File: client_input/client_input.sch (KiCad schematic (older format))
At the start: 21 parts, among them P1 CONN_01X06, P2 CONN_01X08, SW1 DIPS_08, SW2 SW_PUSH, SW3 SW_PUSH, U1 ESP-12_Breakout, U2 MCP23017, U3 MCP3208, U4 WS2812B

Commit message: updated references, added BattSense, fixed errors
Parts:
- removed P?: CONN_01X05, symbol CONN_01X05
- added P7: spare I/O, symbol CONN_01X04
- added R1: 100k, symbol R
- added R2: 22k, symbol R
- added SW4: PAIR_MODE, Buttons_Switches_ThroughHole:SW_TH_Tactile_Omron_B3F-10xx, symbol SW_PUSH
- P1: renamed from P2; value CONN_01X08 -> Analog In
- P2: renamed from P1; value CONN_01X06 -> FTDI
- P3, P4: renamed from P?; value CONN_01X09 -> Ribbon
- P5, P6: renamed from P?; value CONN_01X03 -> Ribbon
- SW2: value SW_PUSH -> RESET
- SW3: value SW_PUSH -> Bootload
- gave numbers to parts that had none: 6
- renumbered U4 to D1, R1 to R3
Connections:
- net labels added: +3V3, Pair_sw
- net labels removed: +3.3V
- wire segments 82 -> 99
- no-connect marks 6 -> 4
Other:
- note removed: "Analog Inputs"
- note removed: "I/O connections"
- moved on the sheet: D1, D2, D3, D4, P1, P2, P3, P4, P5, P6, R3, R4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

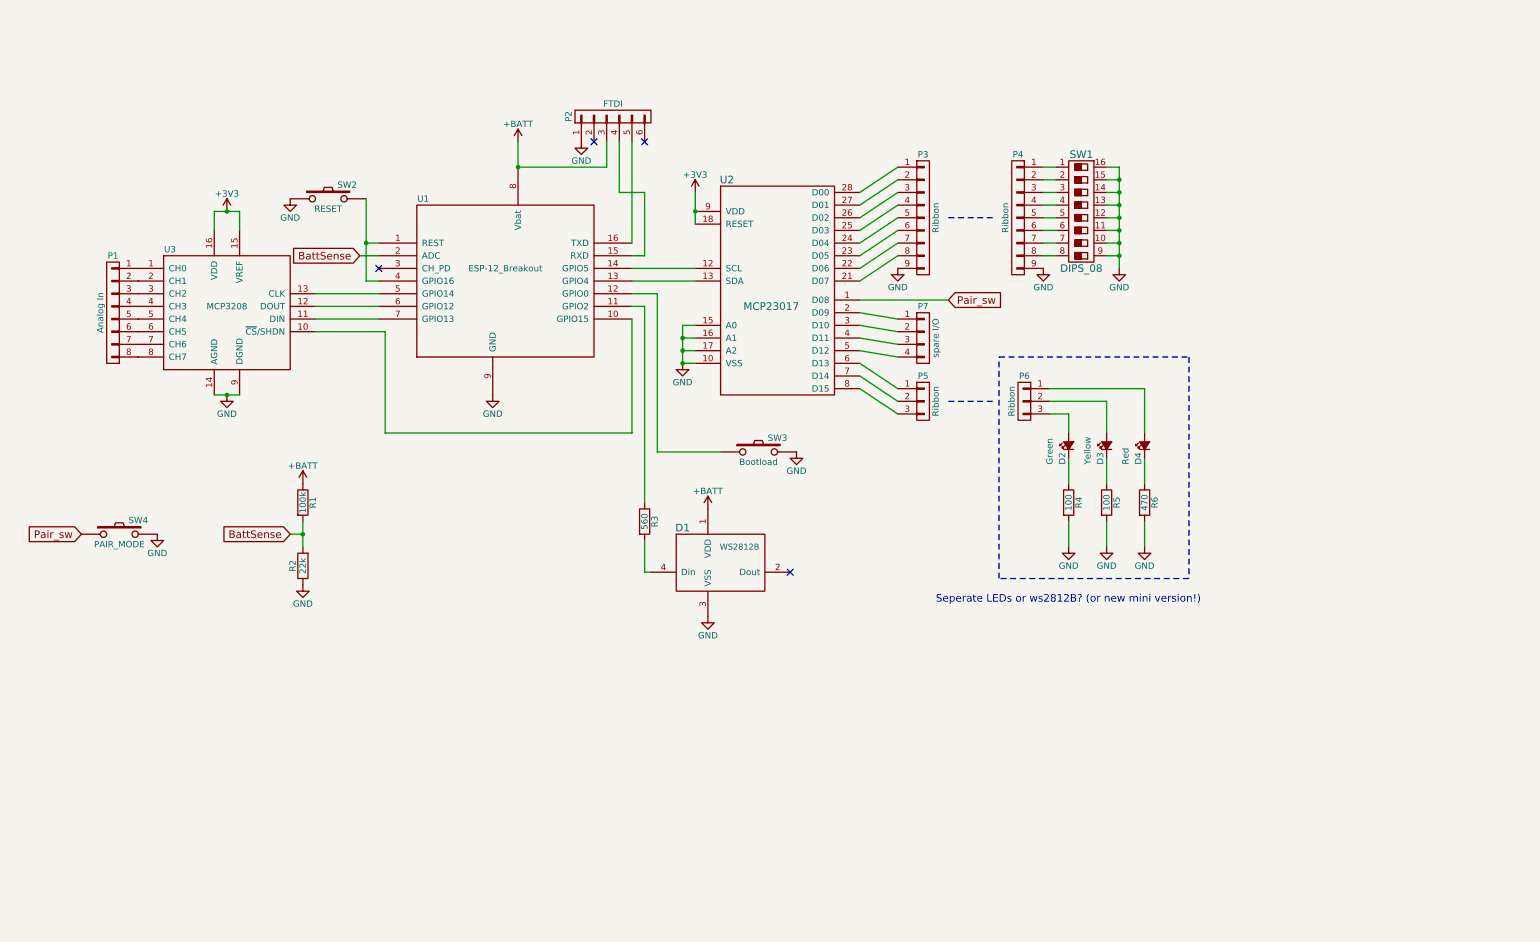
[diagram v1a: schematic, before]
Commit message: add RGB status LED alternative
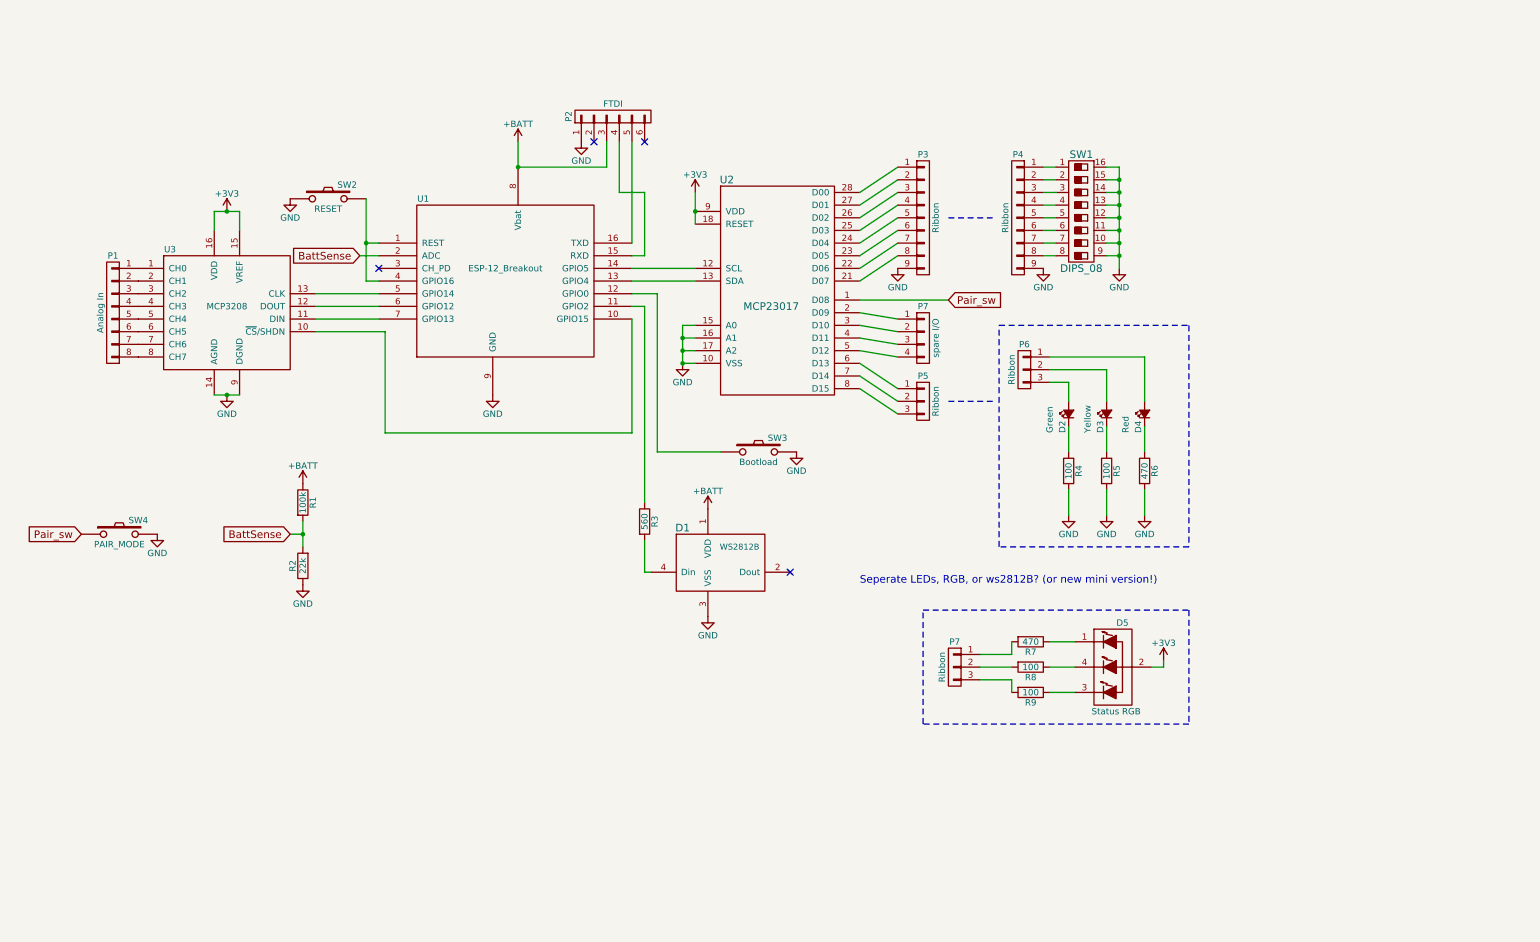
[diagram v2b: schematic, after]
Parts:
- added D5: Status RGB, symbol LED_RABG
- added P7: Ribbon, symbol CONN_01X03
- added R7: 470, symbol R
- added R8, R9: 100, symbol R
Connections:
- net +3V3: now also D5.2 (COMMON_ANODE)
- new net: D5.1 (RED_CATHODE), R7.1
- new net: D5.3 (BLUE_CATHODE), R9.1
- new net: D5.4 (GREEN_CATHODE), R8.1
- new net: P7.1 (P1), R7.2
- new net: P7.2 (P2), R8.2
- new net: P7.3 (P3), R9.2
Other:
- note added: "Seperate LEDs, RGB, or ws2812B? (or new mini version!)"
- note removed: "Seperate LEDs or ws2812B? (or new mini version!)"
- moved on the sheet: D2, D3, D4, P6, R4, R5, R6

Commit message: PCD laid out.
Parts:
- removed P5, P7: Ribbon, symbol CONN_01X03
- removed P7: spare I/O, symbol CONN_01X04
- added P4: Ribbon, symbol CONN_01X08
- added P6: Ribbon, Socket_Strips:Socket_Strip_Straight_1x04, symbol CONN_01X04
- D2, D3: footprint (none) -> LEDs:LED-3MM
- D4: renamed from D5; footprint (none) -> LEDs:LED-RGB-5MM_Common_Cathode
- D5: renamed from D4; footprint (none) -> LEDs:LED-3MM
- P2: footprint Pin_Headers:Pin_Header_Angled_1x06 -> Pin_Headers:Pin_Header_Straight_1x06
- P3: footprint (none) -> Socket_Strips:Socket_Strip_Straight_1x09
- P7: renamed from P4; footprint (none) -> Socket_Strips:Socket_Strip_Straight_1x09
- P8: renamed from P6; footprint (none) -> Socket_Strips:Socket_Strip_Straight_1x03
- R1, R2: footprint (none) -> Resistors_ThroughHole:Resistor_Horizontal_RM10mm
- R4: renamed from R7; footprint (none) -> Resistors_ThroughHole:Resistor_Horizontal_RM10mm
- R5: renamed from R8; footprint (none) -> Resistors_ThroughHole:Resistor_Horizontal_RM10mm
- R6: renamed from R9; footprint (none) -> Resistors_ThroughHole:Resistor_Horizontal_RM10mm
- R7: renamed from R4; footprint (none) -> Resistors_ThroughHole:Resistor_Horizontal_RM10mm
- R8: renamed from R5; footprint (none) -> Resistors_ThroughHole:Resistor_Horizontal_RM10mm
- R9: renamed from R6; footprint (none) -> Resistors_ThroughHole:Resistor_Horizontal_RM10mm
- U1: renamed from U3; footprint Housings_DIP:DIP-18_W7.62mm_LongPads -> Housings_DIP:DIP-16_W7.62mm_LongPads
- renumbered SW4 to SW1, SW1 to SW4, U1 to U2, U2 to U3
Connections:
- net +3V3: now also P4.8 (P8), P6.4 (P4)
- net at U3.2 (D09): now also P4.1 (P1)
- net at U3.3 (D10): now also P4.2 (P2)
- net at U3.4 (D11): now also P4.3 (P3)
- net at U3.5 (D12): now also P4.4 (P4)
- net at U3.6 (D13): now also P4.5 (P5)
- net at U3.7 (D14): now also P4.6 (P6)
- net at U3.8 (D15): now also P4.7 (P7)
- net at R4.2: now also P6.1 (P1)
- net at R5.2: now also P6.3 (P3)
- net at R6.2: now also P6.2 (P2)
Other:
- moved on the sheet: D2, D3, D4, D5, P8, R4, R5, R6, R7, R8, R9

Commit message: Made some tweaks, outputted test gerber files (still PTH version).
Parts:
- added P9: LiPo, Socket_Strips:Socket_Strip_Straight_1x02, symbol CONN_01X02
- D1: footprint LEDs:LED_RGB_PLLC-6 -> LEDs:LED_NEOPIXEL
- P4: footprint (none) -> Socket_Strips:Socket_Strip_Straight_1x08
- R1, R2, R3, R4, R5, R6, R7, R8, R9: footprint Resistors_ThroughHole:Resistor_Horizontal_RM10mm -> Discret:R4
- SW2, SW3: footprint Buttons_Switches_ThroughHole:SW_TH_Tactile_Omron_B3F-10xx -> Buttons_Switches_ThroughHole:SW_PUSH_SMALL
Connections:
- net +BATT: now also P9.2 (P2)
- net GND: now also P9.1 (P1)
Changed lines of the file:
@@
 F 0 "SW3" H 6700 4360 50  0000 C CNN
 F 1 "Bootload" H 6550 4170 50  0000 C CNN
-F 2 "Buttons_Switches_ThroughHole:SW_TH_Tactile_Omron_B3F-10xx" H 6550 4250 50  0001 C CNN
+F 2 "Buttons_Switches_ThroughHole:SW_PUSH_SMALL" H 6550 4250 50  0001 C CNN
 F 3 "" H 6550 4250 50  0000 C CNN
 	1    6550 4250
@@
 F 0 "SW2" H 3300 2360 50  0000 C CNN
 F 1 "RESET" H 3150 2170 50  0000 C CNN
-F 2 "Buttons_Switches_ThroughHole:SW_TH_Tactile_Omron_B3F-10xx" H 3150 2250 50  0001 C CNN
+F 2 "Buttons_Switches_ThroughHole:SW_PUSH_SMALL" H 3150 2250 50  0001 C CNN
 F 3 "" H 3150 2250 50  0000 C CNN
 	1    3150 2250
@@
 F 0 "D1" H 5950 5350 60  0000 C CNN
 F 1 "WS2812B" H 6400 5200 47  0000 C CNN
-F 2 "LEDs:LED_RGB_PLLC-6" H 6300 5150 60  0001 C CNN
+F 2 "LEDs:LED_NEOPIXEL" H 6300 5150 60  0001 C CNN
 F 3 "" H 6300 5150 60  0000 C CNN
 	1    6300 5100
@@
 F 0 "R3" V 5730 4800 50  0000 C CNN
 F 1 "560" V 5650 4800 50  0000 C CNN
-F 2 "Resistors_ThroughHole:Resistor_Horizontal_RM10mm" V 5580 4800 50  0001 C CNN
+F 2 "Discret:R4" V 5580 4800 50  0001 C CNN
 F 3 "" H 5650 4800 50  0000 C CNN
 	1    5650 4800
@@
 F 0 "R8" V 9380 4500 50  0000 C CNN
 F 1 "100" V 9300 4500 50  0000 C CNN
-F 2 "Resistors_ThroughHole:Resistor_Horizontal_RM10mm" V 9230 4500 50  0001 C CNN
+F 2 "Discret:R4" V 9230 4500 50  0001 C CNN
 F 3 "" H 9300 4500 50  0000 C CNN
 	1    9300 4500
@@
 F 0 "R7" V 9080 4500 50  0000 C CNN
 F 1 "100" V 9000 4500 50  0000 C CNN
-F 2 "Resistors_ThroughHole:Resistor_Horizontal_RM10mm" V 8930 4500 50  0001 C CNN
+F 2 "Discret:R4" V 8930 4500 50  0001 C CNN
 F 3 "" H 9000 4500 50  0000 C CNN
 	1    9000 4500
@@
 F 0 "R9" V 9680 4500 50  0000 C CNN
 F 1 "470" V 9600 4500 50  0000 C CNN
-F 2 "Resistors_ThroughHole:Resistor_Horizontal_RM10mm" V 9530 4500 50  0001 C CNN
+F 2 "Discret:R4" V 9530 4500 50  0001 C CNN
 F 3 "" H 9600 4500 50  0000 C CNN
 	1    9600 4500
@@
 F 0 "R1" V 3030 4650 50  0000 C CNN
 F 1 "100k" V 2950 4650 50  0000 C CNN
-F 2 "Resistors_ThroughHole:Resistor_Horizontal_RM10mm" V 2880 4650 50  0001 C CNN
+F 2 "Discret:R4" V 2880 4650 50  0001 C CNN
 F 3 "" H 2950 4650 50  0000 C CNN
 	1    2950 4650
@@
 F 0 "R2" V 3030 5150 50  0000 C CNN
 F 1 "22k" V 2950 5150 50  0000 C CNN
-F 2 "Resistors_ThroughHole:Resistor_Horizontal_RM10mm" V 2880 5150 50  0001 C CNN
+F 2 "Discret:R4" V 2880 5150 50  0001 C CNN
 F 3 "" H 2950 5150 50  0000 C CNN
 	1    2950 5150
@@
 F 0 "R4" V 8780 5850 50  0000 C CNN
 F 1 "470" V 8700 5850 50  0000 C CNN
-F 2 "Resistors_ThroughHole:Resistor_Horizontal_RM10mm" V 8630 5850 50  0001 C CNN
+F 2 "Discret:R4" V 8630 5850 50  0001 C CNN
 F 3 "" H 8700 5850 50  0000 C CNN
 	1    8700 5850
@@
 F 0 "R5" V 8780 6050 50  0000 C CNN
 F 1 "100" V 8700 6050 50  0000 C CNN
-F 2 "Resistors_ThroughHole:Resistor_Horizontal_RM10mm" V 8630 6050 50  0001 C CNN
+F 2 "Discret:R4" V 8630 6050 50  0001 C CNN
 F 3 "" H 8700 6050 50  0000 C CNN
 	1    8700 6050
@@
 F 0 "R6" V 8780 6250 50  0000 C CNN
 F 1 "100" V 8700 6250 50  0000 C CNN
-F 2 "Resistors_ThroughHole:Resistor_Horizontal_RM10mm" V 8630 6250 50  0001 C CNN
+F 2 "Discret:R4" V 8630 6250 50  0001 C CNN
 F 3 "" H 8700 6250 50  0000 C CNN
 	1    8700 6250
@@
 F 0 "P4" H 7850 4150 50  0000 C CNN
 F 1 "Ribbon" V 7950 3700 50  0000 C CNN
-F 2 "" H 7850 3700 50  0000 C CNN
+F 2 "Socket_Strips:Socket_Strip_Straight_1x08" H 7850 3700 50  0001 C CNN
 F 3 "" H 7850 3700 50  0000 C CNN
 	1    7850 3700
@@
 Wire Notes Line
 	7150 6100 7800 6100
+$Comp
+L CONN_01X02 P9
+U 1 1 578040F4
+P 4300 4900
+F 0 "P9" H 4300 5050 50  0000 C CNN
+F 1 "LiPo" V 4400 4900 50  0000 C CNN
+F 2 "Socket_Strips:Socket_Strip_Straight_1x02" H 4300 4900 50  0001 C CNN
+F 3 "" H 4300 4900 50  0000 C CNN
+	1    4300 4900
+	-1   0    0    1
+$EndComp
+$Comp
+L +BATT #PWR024
+U 1 1 57804287
+P 4600 4800
+F 0 "#PWR024" H 4600 4650 50  0001 C CNN
+F 1 "+BATT" H 4600 4940 50  0000 C CNN
+F 2 "" H 4600 4800 50  0000 C CNN
+F 3 "" H 4600 4800 50  0000 C CNN
+	1    4600 4800
+	1    0    0    -1
+$EndComp
+$Comp
+L GND #PWR025
+U 1 1 578042D5
+P 4600 5000
+F 0 "#PWR025" H 4600 4750 50  0001 C CNN
+F 1 "GND" H 4600 4850 50  0000 C CNN
+F 2 "" H 4600 5000 50  0000 C CNN
+F 3 "" H 4600 5000 50  0000 C CNN
+	1    4600 5000
+	1    0    0    -1
+$EndComp
+Wire Wire Line
+	4500 4850 4600 4850
+Wire Wire Line
+	4600 4850 4600 4800
+Wire Wire Line
+	4500 4950 4600 4950
+Wire Wire Line
+	4600 4950 4600 5000
 $EndSCHEMATC

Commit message: ???
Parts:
- removed D2: Green, LEDs:LED-3MM, symbol Led_Small
- removed D3: Yellow, LEDs:LED-3MM, symbol Led_Small
- removed D4: Status RGB, LEDs:LED-RGB-5MM_Common_Cathode, symbol LED_RABG
- removed D5: Red, LEDs:LED-3MM, symbol Led_Small
- removed P6: Ribbon, Socket_Strips:Socket_Strip_Straight_1x04, symbol CONN_01X04
- removed P8: Ribbon, Socket_Strips:Socket_Strip_Straight_1x03, symbol CONN_01X03
- removed R4, R9: 470, Discret:R4, symbol R
- removed R5, R6, R7, R8: 100, Discret:R4, symbol R
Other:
- note removed: "Seperate LEDs, RGB, or ws2812B? (or new mini version!)"

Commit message: version 2.0, lots of changes. (smd parts, 2 sided, production ready)
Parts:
- removed U2: ESP-12_Breakout, ESP8266:ESP12_Breakout, symbol ESP-12_Breakout
- added C1: 2.2uF, Capacitors_ThroughHole:C_Disc_D3_P2.5, symbol C
- added P2: Analog In, Socket_Strips:Socket_Strip_Straight_1x08, symbol CONN_01X08
- added P3: SS, Measurement_Points:Measurement_Point_Round-TH_Small, symbol CONN_01X01
- added P8, P9: Ribbon, Socket_Strips:Socket_Strip_Straight_1x09, symbol CONN_01X09
- added R1: 10k, Discret:R4, symbol R
- added RR1: RR5, Resistors_ThroughHole:Resistor_Array_SIP5, symbol RR5
- added SW5: SPDT, Buttons_Switches_ThroughHole:SW_Micro_SPST, symbol Switch_SPDT_x2
- added U2: MCP3208, Housings_SOIC:SOIC-16_3.9x9.9mm_Pitch1.27mm, symbol MCP3008
- added U3: ESP-12E, ESP8266:ESP-12E_Brendan, symbol ESP-12
- added U4: MCP1700-3302, TO_SOT_Packages_SMD:SOT89-3_Housing_Handsoldering, symbol MCP1700-3302
- added U6: MCP23017, Housings_SOIC:SOIC-28_7.5x17.9mm_Pitch1.27mm, symbol MCP23017
- SW2: renamed from SW1; footprint Buttons_Switches_ThroughHole:SW_TH_Tactile_Omron_B3F-10xx -> Buttons_Switches_ThroughHole:SW_PUSH_SMALL
- U1: footprint Housings_DIP:DIP-16_W7.62mm_LongPads -> Housings_SOIC:SOIC-16_3.9x9.9mm_Pitch1.27mm
- U5: renamed from U3; footprint Housings_DIP:DIP-28_W7.62mm_LongPads -> Housings_SOIC:SOIC-28_7.5x17.9mm_Pitch1.27mm
- renumbered P7 to P10, P2 to P4, P9 to P5, P3 to P6, P4 to P7, R3 to R2, R1 to R3, R2 to R4, SW2 to SW1
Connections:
- net +3V3: now also C1.1, P9.9 (P9), RR1.1 (COM), U2.15 (VREF), U2.16 (VDD), U3.8 (VCC), U4.3 (Vout), U6.15 (A0), U6.18 (RESET), U6.9 (VDD)
- net +BATT: now also SW5.1 (A); no longer D1.1 (VDD), P4.3 (P3)
- net BattSense: now also U3.2 (ADC)
- net GND: now also SW1.2, C1.2, P8.9 (P9), R1.2, U2.14 (AGND), U2.9 (DGND), U3.9 (GND), U4.1 (GND), U6.10 (VSS), U6.16 (A1), U6.17 (A2); no longer SW1.1
- net SPI_SS: now reaches U1.10 (~CS~/SHDN)
- net SPI_SS: now also R1.1, U3.10 (GPIO15)
- net MOSI: now reaches U1.11 (DIN)
- net MOSI: now also U2.11 (DIN), U3.7 (GPIO13)
- net MISO: now reaches U1.12 (DOUT)
- net MISO: now also U2.12 (DOUT), U3.6 (GPIO12)
- net SPI_CLK: now reaches U1.13 (CLK)
- net SPI_CLK: now also U2.13 (CLK), U3.5 (GPIO14)
- net LED_stat: now reaches R2.1
- net LED_stat: now also U3.11 (GPIO2)
- net BL_sw: now reaches SW3.1
- net BL_sw: now also RR1.2, U3.12 (GPIO0)
- net SDA: now reaches U5.13 (SDA)
- net SDA: now also U3.13 (GPIO4), U6.13 (SDA)
- net SCL: now reaches U5.12 (SCL)
- net SCL: now also U3.14 (GPIO5), U6.12 (SCL)
- net at P4.4 (P4): now also U3.15 (RXD)
- net at P4.5 (P5): now also U3.16 (TXD)
- new net: P9.1 (P1), U6.1 (D08)
- new net: P9.2 (P2), U6.2 (D09)
- new net: P8.8 (P8), U6.21 (D07)
- new net: P8.7 (P7), U6.22 (D06)
- new net: P8.6 (P6), U6.23 (D05)
- new net: P8.5 (P5), U6.24 (D04)
- new net: P8.4 (P4), U6.25 (D03)
- new net: P8.3 (P3), U6.26 (D02)
- new net: P8.2 (P2), U6.27 (D01)
- new net: P8.1 (P1), U6.28 (D00)
- new net: P9.3 (P3), U6.3 (D10)
- new net: P9.4 (P4), U6.4 (D11)
- new net: P9.5 (P5), U6.5 (D12)
- new net: P9.6 (P6), U6.6 (D13)
- new net: P9.7 (P7), U6.7 (D14)
- new net: P9.8 (P8), U6.8 (D15)
- new net: P2.1 (P1), U2.1 (CH0)
- new net: P3.1 (P1), U2.10 (~CS~/SHDN)
- new net: P2.2 (P2), U2.2 (CH1)
- new net: P2.3 (P3), U2.3 (CH2)
- new net: P2.4 (P4), U2.4 (CH3)
- new net: P2.5 (P5), U2.5 (CH4)
- new net: P2.6 (P6), U2.6 (CH5)
- new net: P2.7 (P7), U2.7 (CH6)
- new net: P2.8 (P8), U2.8 (CH7)
- new net +Vin: D1.1 (VDD), SW5.2 (B), U4.2 (Vin)
- new net CH_PD: RR1.3, U3.3 (CH_PD)
- new net FTDI_VCC: P4.3 (P3), SW5.3 (C)
- new net RST: RR1.4, SW1.1, U3.1 (REST), U3.4 (GPIO16)
- no-connect marks 4 -> 5
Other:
- moved on the sheet: D1, P1, P10, P4, P5, P6, P7, R2, R3, R4, SW1, SW2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
